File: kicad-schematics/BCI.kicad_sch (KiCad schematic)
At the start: 27 parts, among them U1 AD620

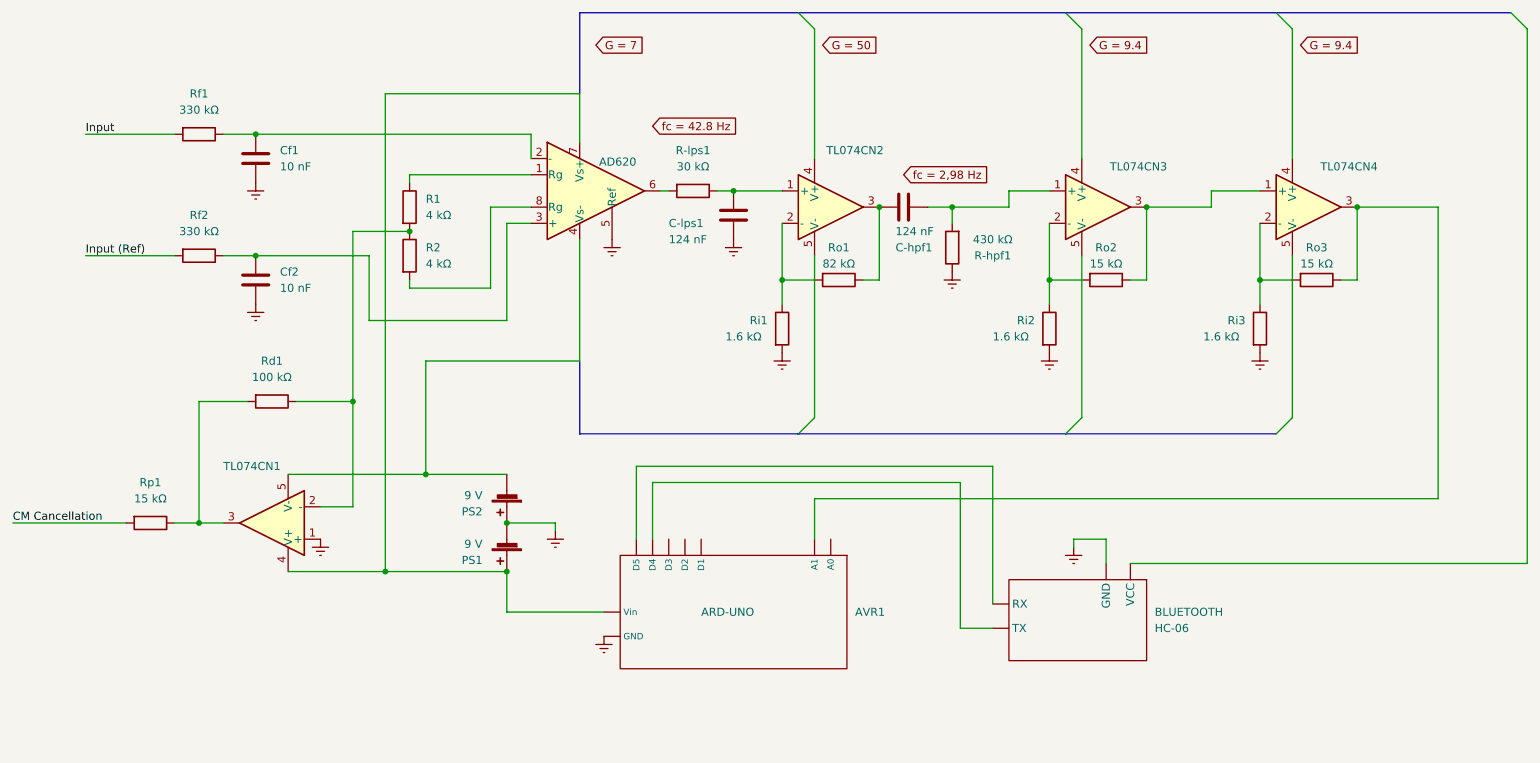
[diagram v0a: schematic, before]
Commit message: Adding new schematic
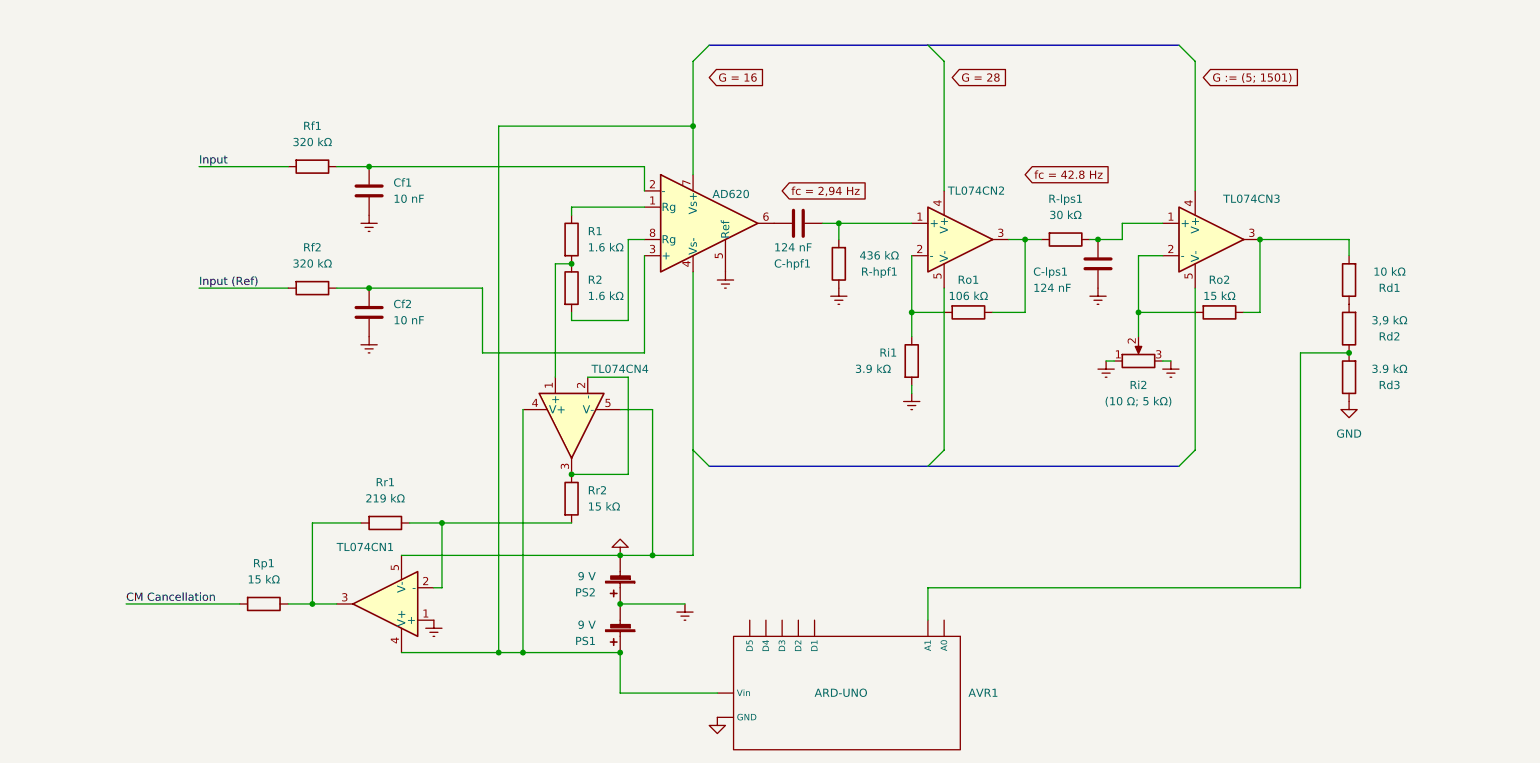
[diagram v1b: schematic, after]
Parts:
- removed BLUETOOTH: HC-06, symbol HC06:HC-06
- removed Ri2, Ri3: 1.6 kΩ, Resistor_THT:R_Axial_DIN0204_L3.6mm_D1.6mm_P1.90mm_Vertical, symbol Device:R
- removed Ro3: 15 kΩ, Resistor_THT:R_Axial_DIN0204_L3.6mm_D1.6mm_P1.90mm_Vertical, symbol Device:R
- added Rd1: 10 kΩ, Resistor_THT:R_Axial_DIN0204_L3.6mm_D1.6mm_P1.90mm_Vertical, symbol Device:R
- added Rd2: 3,9 kΩ, Resistor_THT:R_Axial_DIN0204_L3.6mm_D1.6mm_P1.90mm_Vertical, symbol Device:R
- added Rd3: 3.9 kΩ, Resistor_THT:R_Axial_DIN0204_L3.6mm_D1.6mm_P1.90mm_Vertical, symbol Device:R
- added Ri2: (10 Ω; 5 kΩ), symbol Device:R_Potentiometer
- added Rr2: 15 kΩ, Resistor_THT:R_Axial_DIN0204_L3.6mm_D1.6mm_P1.90mm_Vertical, symbol Device:R
- R-hpf1: value 430 kΩ -> 436 kΩ
- R1, R2: value 4 kΩ -> 1.6 kΩ
- Rf1, Rf2: value 330 kΩ -> 320 kΩ
- Ri1: value 1.6 kΩ -> 3.9 kΩ
- Ro1: value 82 kΩ -> 106 kΩ
- Rr1: renamed from Rd1; value 100 kΩ -> 219 kΩ
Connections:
- net Earth: now also Ri2.1, Ri2.3; no longer AVR1. (Vin)
- net at Ro2.1, TL074CN3.3: now also Rd1.2; no longer TL074CN4.1 (+)
- net at Ro2.2, TL074CN3.2 (-): now also Ri2.2
- net at C-lps1.1, R-lps1.1: now also TL074CN3.1 (+); no longer TL074CN2.1 (+)
- net at R-lps1.2: now also Ro1.1, TL074CN2.3; no longer U1.6
- net GND: now reaches AVR1. (Vin)
- net GND: now also PS2.2 (-), TL074CN1.5 (V-), TL074CN4.5 (V-), U1.4 (Vs-), Rd3.1
- net at TL074CN4.3: now also TL074CN4.2 (-), Rr2.1; no longer AVR1. (Vin)
- net at AVR1. (Vin), PS1.1 (+), TL074CN1.4 (V+)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: now also TL074CN4.4 (V+)
- net at R1.2, R2.1: now also TL074CN4.1 (+); no longer Rr1.1, TL074CN1.2 (-)
- net at C-hpf1.1, R-hpf1.2: now also TL074CN2.1 (+); no longer TL074CN3.1 (+)
- new net: AVR1. (Vin), Rd2.1, Rd3.2
- new net: Rr1.1, Rr2.2, TL074CN1.2 (-)
- new net: Rd1.1, Rd2.2
- new net: C-hpf1.2, U1.6
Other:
- moved on the sheet: AVR1, C-hpf1, C-lps1, Cf1, Cf2, PS1, PS2, R-hpf1, R-lps1, R1, R2, Rf1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
